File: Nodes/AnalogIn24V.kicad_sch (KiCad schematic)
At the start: 33 parts, among them T10 Conn_01x01, T11 Conn_01x01, T9 Conn_01x01, U5 LM358BAIDR, U6 LM358BAIDR

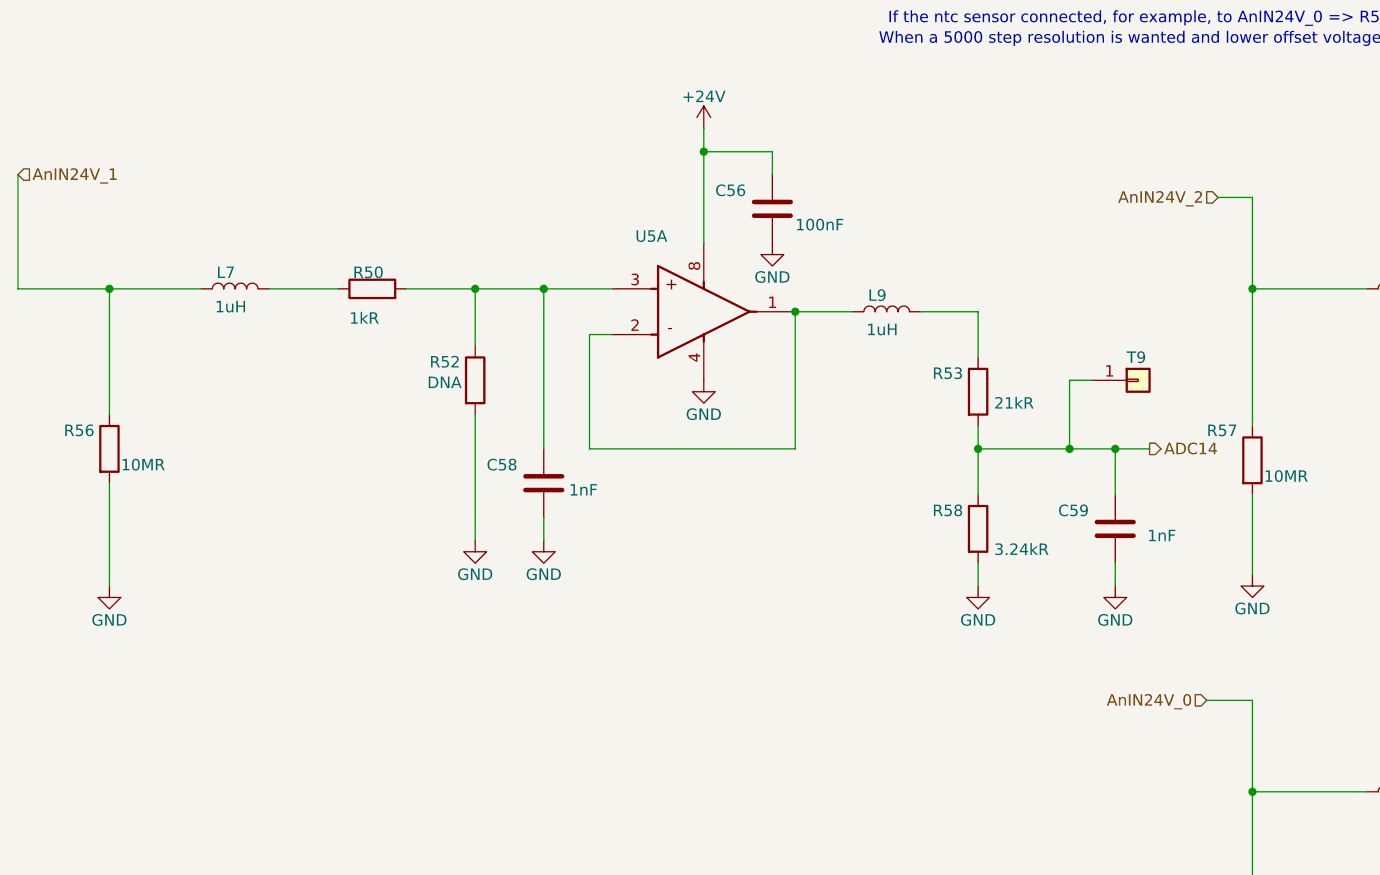
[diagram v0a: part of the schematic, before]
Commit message: Nodes v2.1.2 Improved
- Improved schematic design
- Added two 4.7 uF caps according to the datasheets of the microchips
- Other small changes
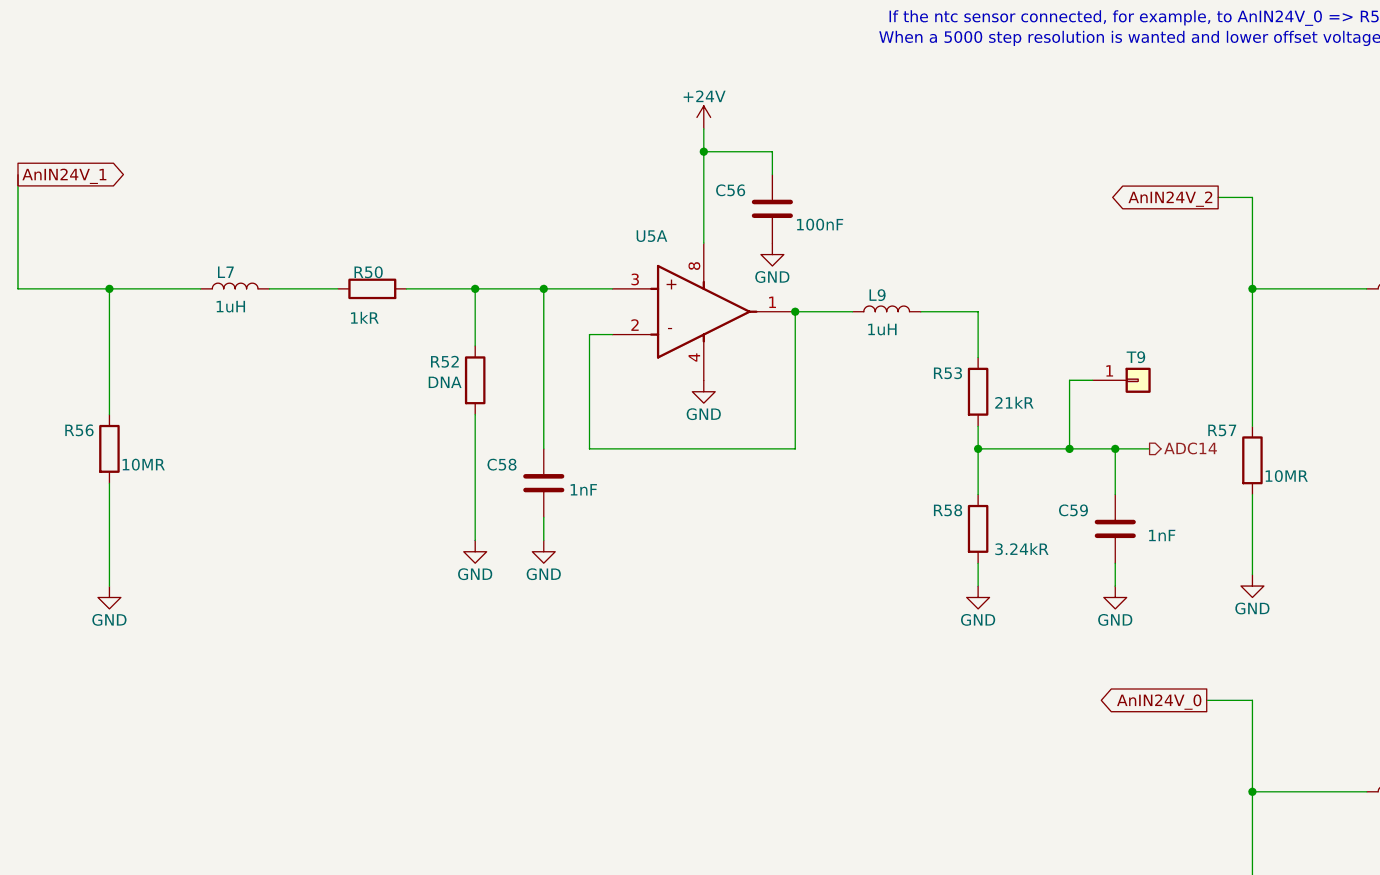
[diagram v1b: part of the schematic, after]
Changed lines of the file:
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@@
 		)
 	)
-	(hierarchical_label "ADC14"
+	(global_label "AnIN24V_1"
 		(shape output)
-		(at 144.78 66.04 0)
+		(at 19.05 35.56 0)
 		(fields_autoplaced yes)
 		(effects
@@
 			(justify left)
 		)
+		(property "Intersheetrefs" "${INTERSHEET_REFS}"
+			(at 31.8928 35.56 0)
+			(effects
+				(font
+					(size 1.27 1.27)
+				)
+				(justify left)
+				(hide yes)
+			)
+		)
 	)
-	(hierarchical_label "AnIN24V_0"
-		(shape input)
+	(global_label "AnIN24V_2"
+		(shape output)
+		(at 152.4 38.1 180)
+		(fields_autoplaced yes)
+		(effects
+			(font
+				(size 1.27 1.27)
+			)
+			(justify right)
+		)
+		(property "Intersheetrefs" "${INTERSHEET_REFS}"
+			(at 139.5572 38.1 0)
+			(effects
+				(font
+					(size 1.27 1.27)
+				)
+				(justify right)
+				(hide yes)
+			)
+		)
+	)
+	(global_label "AnIN24V_0"
+		(shape output)
 		(at 151.13 93.98 180)
 		(fields_autoplaced yes)
@@
 			(justify right)
 		)
+		(property "Intersheetrefs" "${INTERSHEET_REFS}"
+			(at 138.2872 93.98 0)
+			(effects
+				(font
+					(size 1.27 1.27)
+				)
+				(justify right)
+				(hide yes)
+			)
+		)
 	)
-	(hierarchical_label "AnIN24V_2"
-		(shape input)
-		(at 152.4 38.1 180)
+	(hierarchical_label "ADC14"
+		(shape output)
+		(at 144.78 66.04 0)
 		(fields_autoplaced yes)
 		(effects
-			(font
-				(size 1.27 1.27)
-			)
-			(justify right)
-		)
-	)
-	(hierarchical_label "AnIN24V_1"
-		(shape input)
-		(at 19.05 35.56 0)
-		(fields_autoplaced yes)
-		(effects

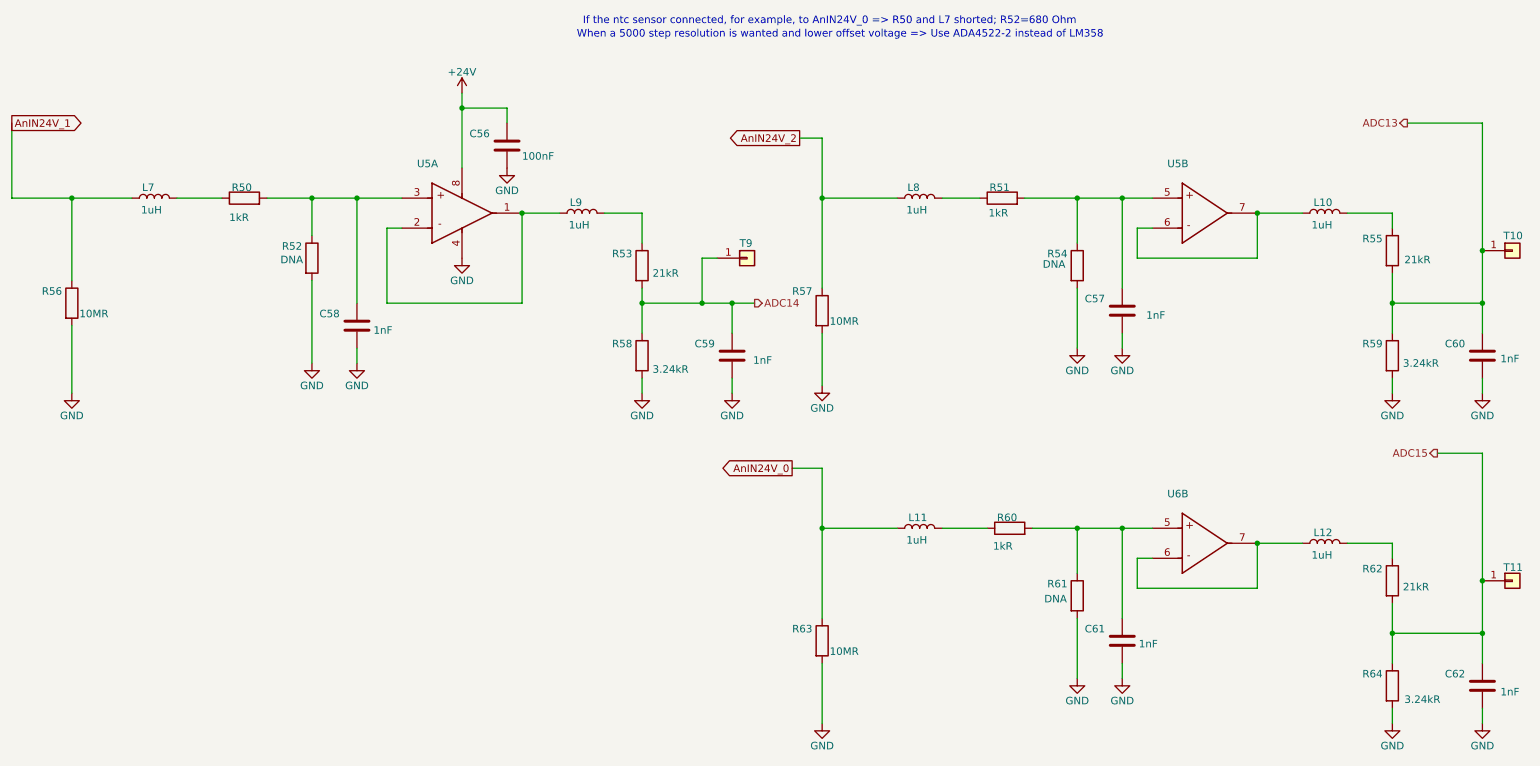
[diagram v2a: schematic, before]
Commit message: Nodes v2.2.5
- New High-Side Driver (Same footprint, just new info)
- Two resistors added for 3V3 Filters, which can be used to implement voltage divider
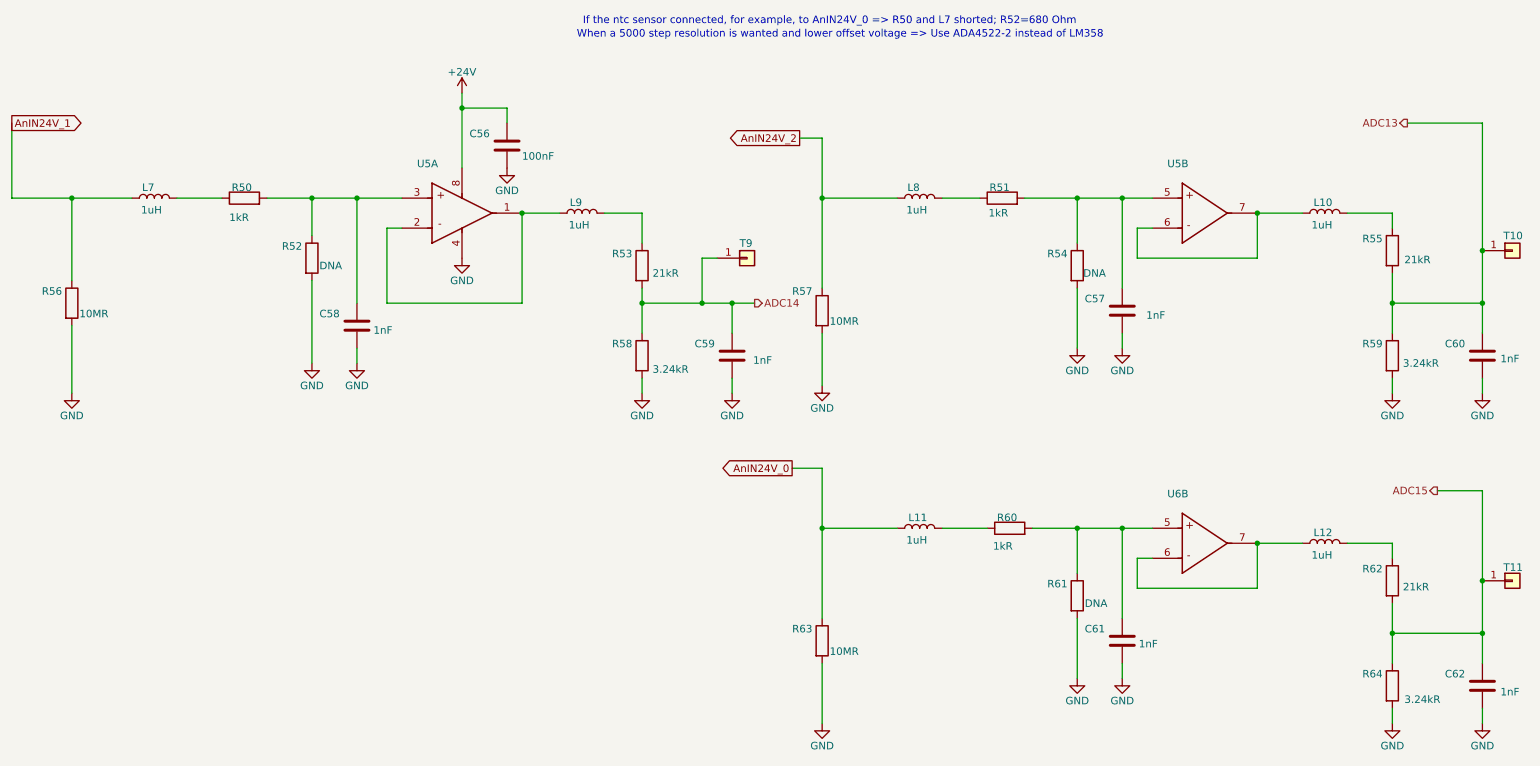
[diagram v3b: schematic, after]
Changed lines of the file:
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@@
 	(wire
 		(pts
-			(xy 260.35 91.44) (xy 267.97 91.44)
+			(xy 260.35 97.79) (xy 267.97 97.79)
 		)
 		(stroke
@@
 	(wire
 		(pts
-			(xy 267.97 91.44) (xy 267.97 113.03)
+			(xy 267.97 97.79) (xy 267.97 113.03)
 		)
 		(stroke
@@
 	(hierarchical_label "ADC15"
 		(shape output)
-		(at 260.35 91.44 180)
+		(at 260.35 97.79 180)
 		(fields_autoplaced yes)
 		(effects
@@
 		)
 		(property "Value" "DNA"
-			(at 193.548 60.198 0)
+			(at 200.406 61.722 0)
 			(effects
 				(font
@@
 		)
 		(property "Value" "DNA"
-			(at 64.516 59.436 0)
+			(at 71.12 60.452 0)
 			(effects
 				(font
@@
 		)
 		(property "Value" "DNA"
-			(at 193.802 116.84 0)
+			(at 200.66 117.602 0)
 			(effects
 				(font

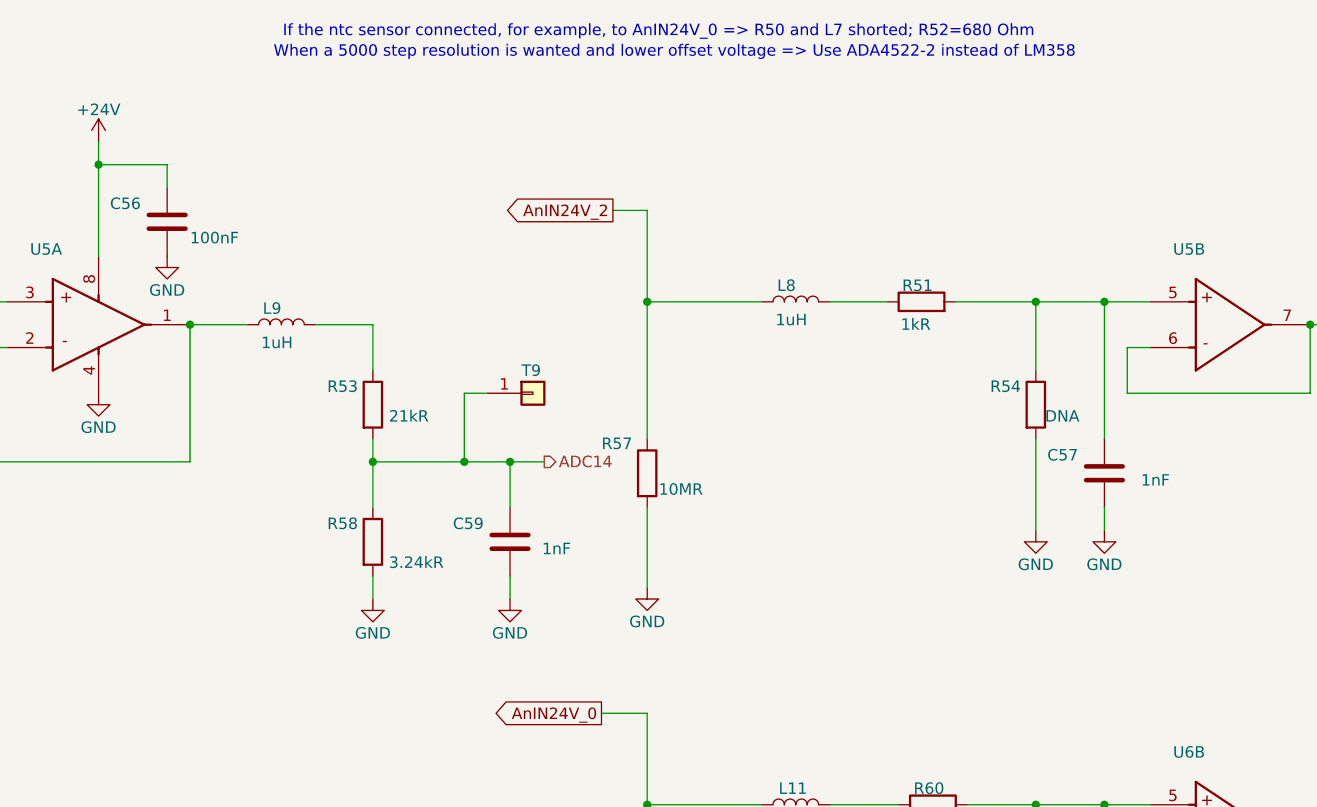
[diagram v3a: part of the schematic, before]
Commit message: Nodes 2.2.5 Revision 1
- New LED colour coding
- Nodes Datasheet added
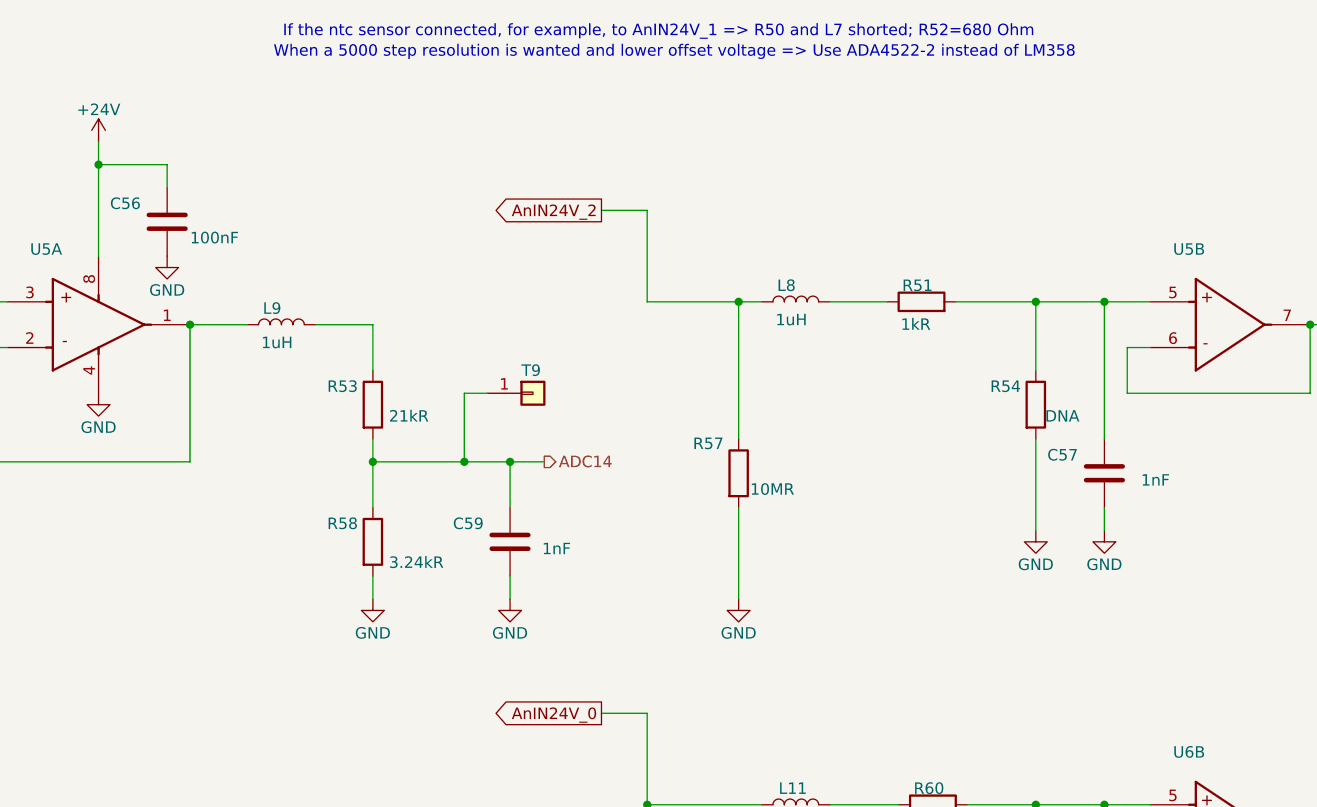
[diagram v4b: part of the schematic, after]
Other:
- note added: "If the ntc sensor connected, for example, to AnIN24V_1 => R50 and L7 shorted; R52=680 Ohm"
- note removed: "If the ntc sensor connected, for example, to AnIN24V_0 => R50 and L7 shorted; R52=680 Ohm"
- moved on the sheet: R57
